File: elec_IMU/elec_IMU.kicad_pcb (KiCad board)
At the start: 4 copper layers, 0 parts

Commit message: [update] Full schematic + positionning
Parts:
- added C1: 100n 6V3, Capacitor_SMD:C_0402_1005Metric, F.Cu at (152.2, 74.8)
- added C2: 100n 6V3, Capacitor_SMD:C_0402_1005Metric, F.Cu at (152.2, 72.8)
- added D1: SP0503BAHT, Package_TO_SOT_SMD:SOT-143, F.Cu at (143.7, 74.5)
- added FID1: DNP Fiducial, Fiducial:Fiducial_1mm_Mask2mm, F.Cu at (101.9, 75.1)
- added FID2: DNP Fiducial, Fiducial:Fiducial_1mm_Mask2mm, F.Cu at (101.9, 78.6)
- added FID3: DNP Fiducial, Fiducial:Fiducial_1mm_Mask2mm, F.Cu at (101.9, 82.2)
- added G1: qwiic_Logo, Library_Pollen:Logo_qwiic_5mm, F.Cu at (110.0, 65.3)
- added H2: Logo HF 2025, Library_Pollen:Logo_HF_2025, F.Cu at (113.6, 70.9)
- added H3: DNP Logo Pollen 2021, Library_Pollen:Logo_Pollen_2021_sq, F.Cu at (105.8, 69.8)
- added H4: Mounting Holes M2,5, MountingHole:MountingHole_2.7mm_M2.5_ISO7380_Pad_TopBottom, F.Cu at (150.4, 67.6)
- added H5: MountingHole_Pad, MountingHole:MountingHole_2.7mm_M2.5_ISO7380_Pad_TopBottom, F.Cu at (137.4, 81.6)
- added H6: Centering Hole 2 mm, Library_Pollen:MountingHole_2.0mm, F.Cu at (137.4, 67.6)
- added H7: Centering Hole 2 mm, Library_Pollen:MountingHole_2.0mm, F.Cu at (150.4, 81.6)
- added J1: JST SH, Connector_JST:JST_SH_SM04B-SRSS-TB_1x04-1MP_P1.00mm_Horizontal, F.Cu at (144.4, 80.7)
- added J2: JST SH, Connector_JST:JST_SH_SM04B-SRSS-TB_1x04-1MP_P1.00mm_Horizontal, F.Cu at (138.4, 74.7)
- added R1: 0R, Resistor_SMD:R_0402_1005Metric, F.Cu at (147.4, 72.1)
- added R2: 0R, Resistor_SMD:R_0402_1005Metric, F.Cu at (146.4, 75.3)
- added R3: DNP-10k, Resistor_SMD:R_0402_1005Metric, F.Cu at (151.2, 76.8)
- added R4: DNP-10k, Resistor_SMD:R_0402_1005Metric, F.Cu at (148.4, 76.9)
- added TP1: TestPoint, TestPoint:TestPoint_Loop_D2.50mm_Drill1.0mm_LowProfile, F.Cu at (144.9, 70.6)
- added U1: BMI088, Package_LGA:Bosch_LGA-16_4.5x3mm_P0.5mm_LayoutBorder7x1y_ClockwisePinNumbering, F.Cu at (149.8, 73.8)
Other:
- board outline added: 19 x 20 mm
- copper layers 4 -> 2

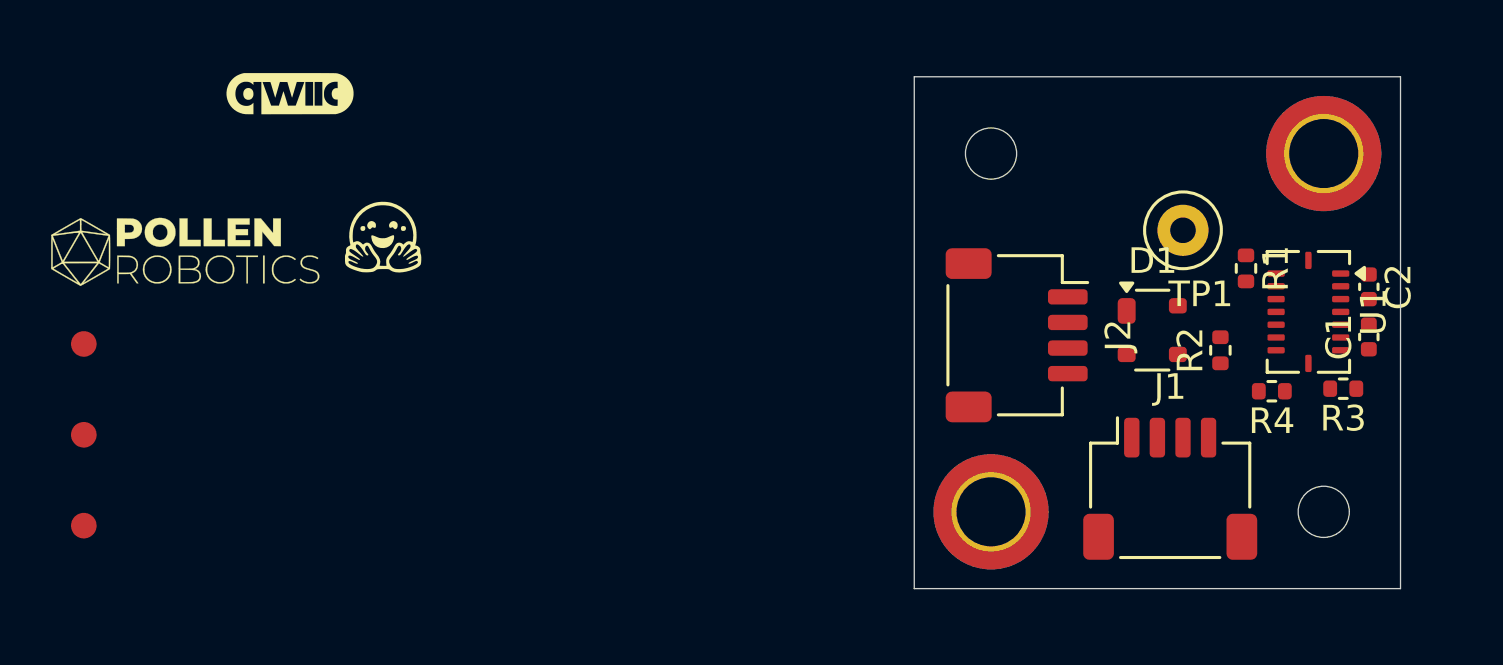
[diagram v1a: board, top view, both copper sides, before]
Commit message: [update] Angle+IMU are routed ERC OK
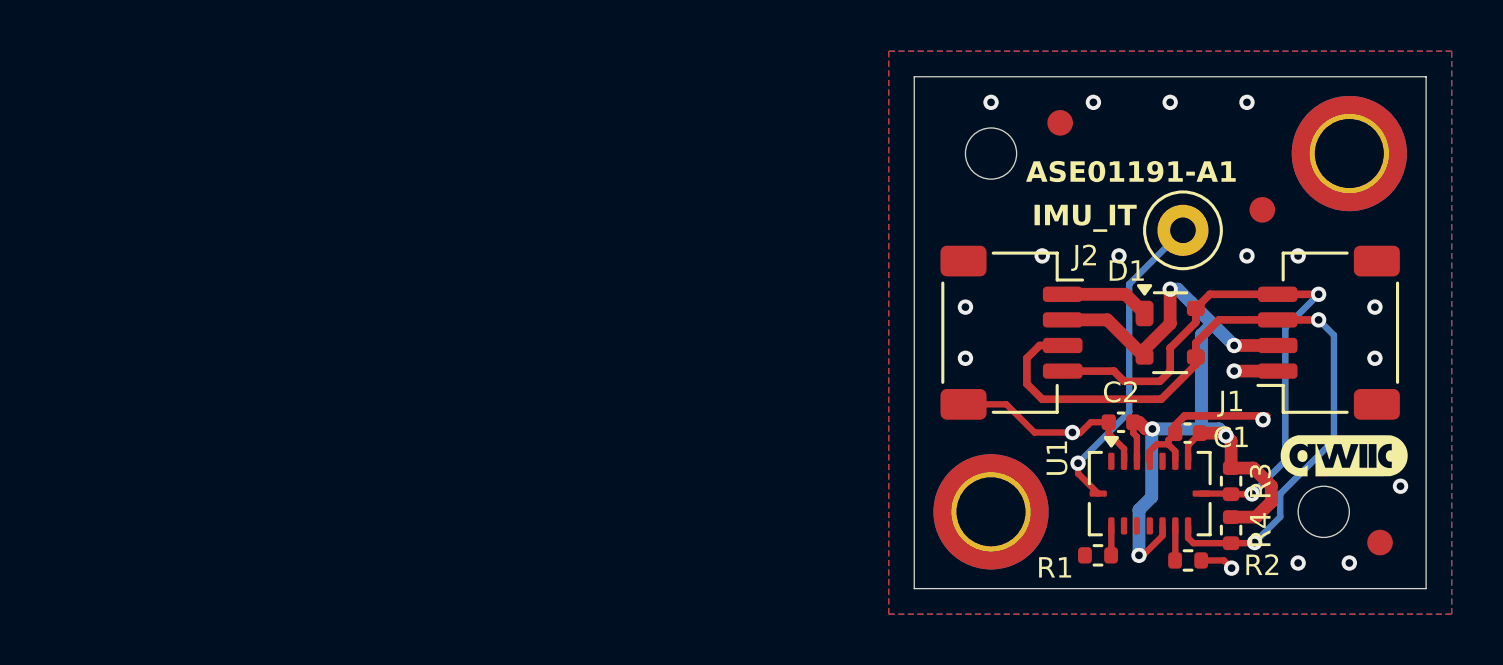
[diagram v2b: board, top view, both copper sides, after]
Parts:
- H2, H3: moved to B.Cu
- moved FID1 51.2 mm to (152.6, 82.8)
- moved FID2 46.9 mm to (148.0, 69.8)
- moved G1 43.6 mm to (151.2, 79.4)
- moved FID3 41.3 mm to (140.1, 66.4)
- moved H2 37.7 mm to (151.0, 75.8), turned to 180 degrees
- moved H3 35.2 mm to (140.7, 74.0), turned to 180 degrees
- moved R1 12.6 mm to (141.6, 83.3), turned to 0 degrees
- moved C2 11.0 mm to (142.5, 78.1), turned to 0 degrees
- moved U1 9.43 mm to (143.6, 80.9), turned to 0 degrees
- moved J1 8.70 mm to (150.6, 74.6), turned to 90 degrees
- moved R2 8.31 mm to (145.1, 83.5), turned to 180 degrees
- moved C1 8.02 mm to (145.1, 78.6), turned to 180 degrees
- moved R3 5.68 mm to (146.8, 80.4), turned to -90 degrees
- moved R4 5.66 mm to (146.8, 82.4), turned to -90 degrees
- moved H4 1.00 mm to (151.4, 67.6)
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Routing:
- net +3V3: track 0.00 -> 36.2 mm, vias 0 -> 5
- net Net-(J1-Pin_3): track 0.00 -> 29.4 mm, vias 0 -> 2
- net Net-(J1-Pin_4): track 0.00 -> 23.3 mm, vias 0 -> 2
- net GND: track 0.00 -> 21.3 mm, vias 0 -> 19
- net Net-(U1-INT1): track 0.00 -> 12.3 mm, vias 0 -> 1
- net Net-(U1-SDO2): track 0.00 -> 1.35 mm
- net Net-(U1-SDO1): track 0.00 -> 1.15 mm
- added copper zone on B.Cu, net GND
- added copper zone on F.Cu, net GND
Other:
- board size 19 x 20 mm -> 20 x 20 mm
- board text added: "ASE01191-A1"
- board text added: "IMU_IT"

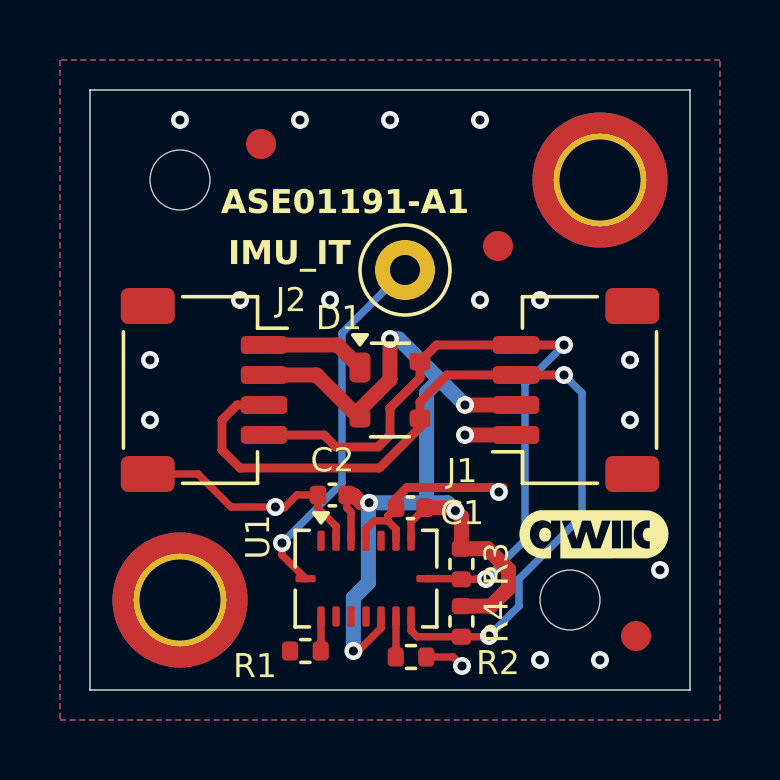
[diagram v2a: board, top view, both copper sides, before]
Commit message: [update] Mechanical adaptations.
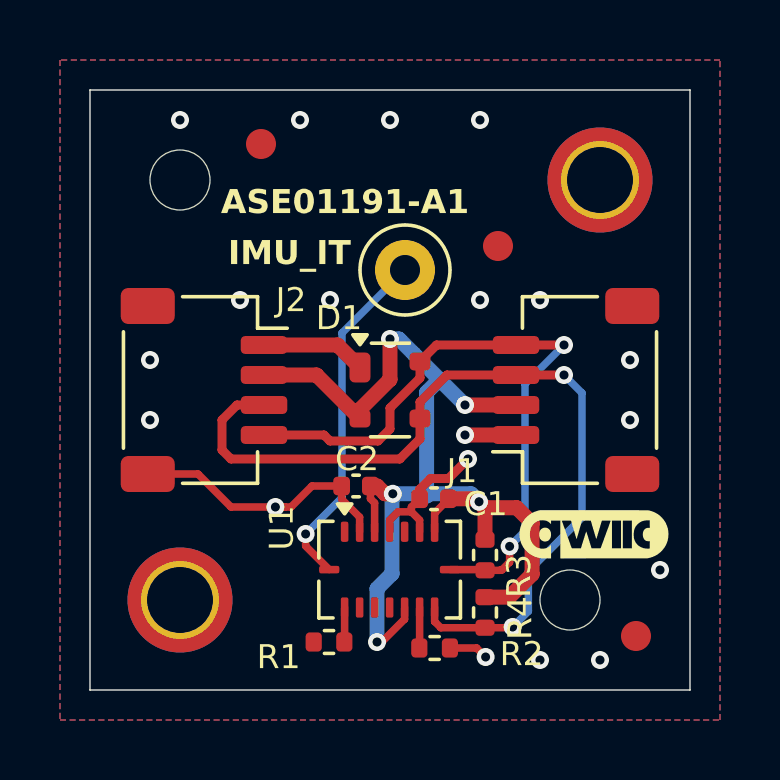
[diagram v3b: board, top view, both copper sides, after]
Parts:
- H4: value Mounting Holes M2,5 -> Mounting Holes M2; footprint MountingHole:MountingHole_2.7mm_M2.5_ISO7380_Pad_TopBottom -> MountingHole:MountingHole_2.2mm_M2_ISO7380_Pad_TopBottom
- H5: value MountingHole_Pad -> Mounting Holes M2; footprint MountingHole:MountingHole_2.7mm_M2.5_ISO7380_Pad_TopBottom -> MountingHole:MountingHole_2.2mm_M2_ISO7380_Pad_TopBottom
- moved C2 0.84 mm to (143.3, 77.8)
- moved U1 0.84 mm to (144.4, 80.6)
- moved C1 0.84 mm to (145.9, 78.3)
- moved R1 0.84 mm to (142.4, 83.0)
- moved R2 0.84 mm to (145.9, 83.2)
- moved R3 0.84 mm to (147.6, 80.1)
- moved R4 0.84 mm to (147.6, 82.1)
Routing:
- net +3V3: track 36.2 -> 37.3 mm
- net Net-(J1-Pin_4): track 23.3 -> 22.2 mm
- net GND: track 21.3 -> 20.4 mm
- net Net-(J1-Pin_3): track 29.4 -> 28.8 mm
- net Net-(U1-INT1): track 12.3 -> 11.7 mm
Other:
- board text added: "x"
- board text added: "y"
- board text added: "z"
